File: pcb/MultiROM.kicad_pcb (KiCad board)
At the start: 2 copper layers, 85.1 x 62.9 mm, 7 parts, among them J1 Conn_02x22_Row_Letter_First, SW1 SW_DIP_x04, U1 SST39SF010, U2 GAL16V8

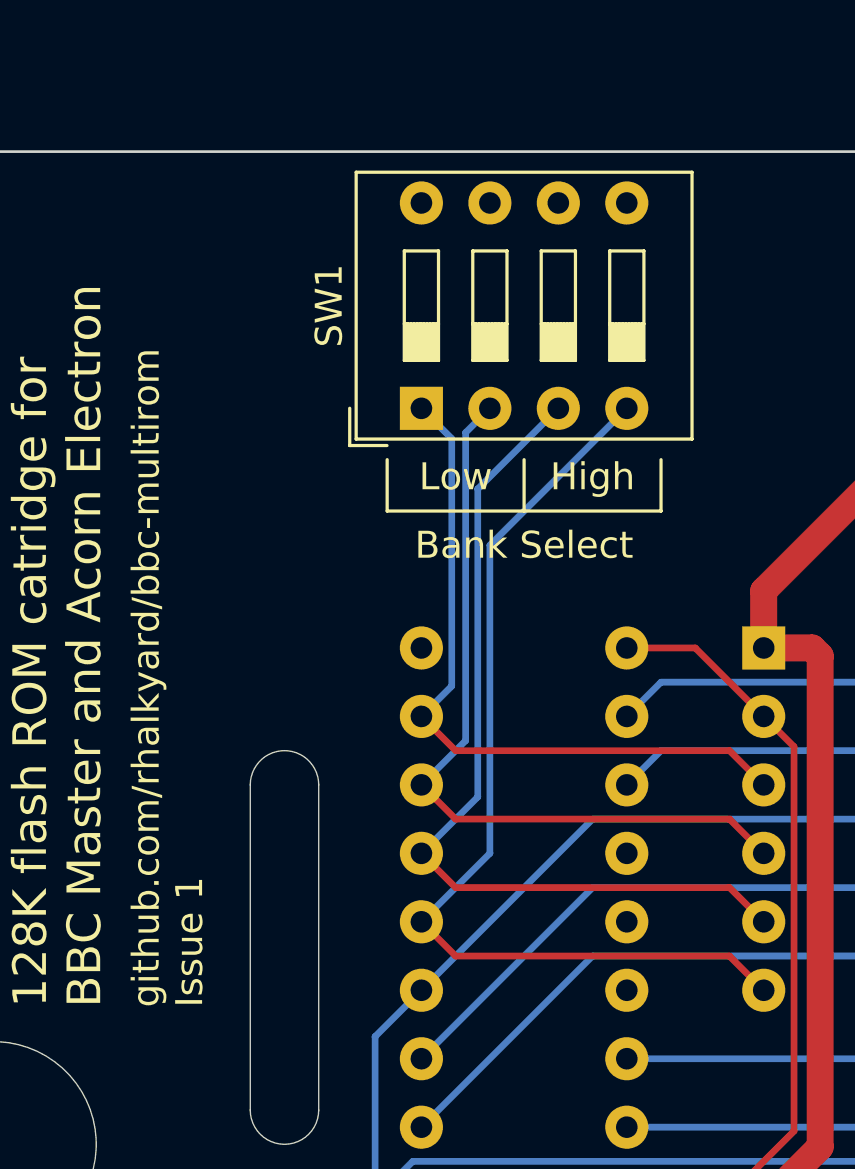
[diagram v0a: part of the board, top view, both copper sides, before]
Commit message: Use edge-style DIP switch
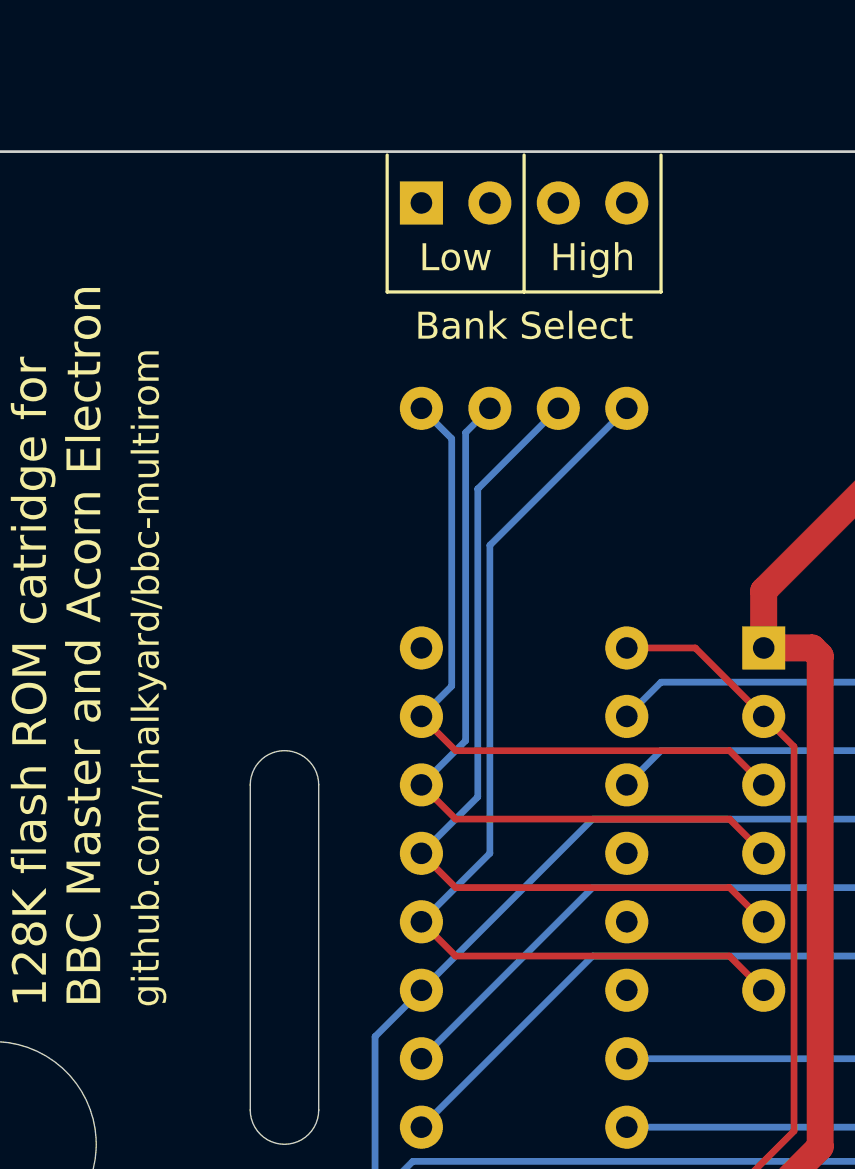
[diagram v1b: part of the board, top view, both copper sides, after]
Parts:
- SW1: footprint Button_Switch_THT:SW_DIP_SPSTx04_Slide_9.78x12.34mm_W7.62mm_P2.54mm -> Button_Switch_THT:SW_DIP_SPSTx04_Piano_10.8x11.72mm_W7.62mm_P2.54mm; moved to B.Cu
- moved SW1 7.62 mm to (47.0, 27.9), turned to -90 degrees
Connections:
- SW1 pad 1: /~{Lo_A16} -> GND
- SW1 pad 2: /~{Lo_A15} -> GND
- SW1 pad 3: /~{Hi_A16} -> GND
- SW1 pad 4: /~{Hi_A15} -> GND
- SW1 pad 5: GND -> /~{Hi_A15}
- SW1 pad 6: GND -> /~{Hi_A16}
- SW1 pad 7: GND -> /~{Lo_A15}
- SW1 pad 8: GND -> /~{Lo_A16}
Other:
- board text added: "github.com/rhalkyard/bbc-multirom"
- board text removed: "github.com/rhalkyard/bbc-multirom Issue 1"
